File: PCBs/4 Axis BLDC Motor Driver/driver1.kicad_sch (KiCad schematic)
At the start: 13 parts, among them Q1 NMOS, Q2 NMOS, Q3 NMOS, Q4 NMOS, Q5 NMOS, Q6 NMOS, U2 DRV8301DCAR

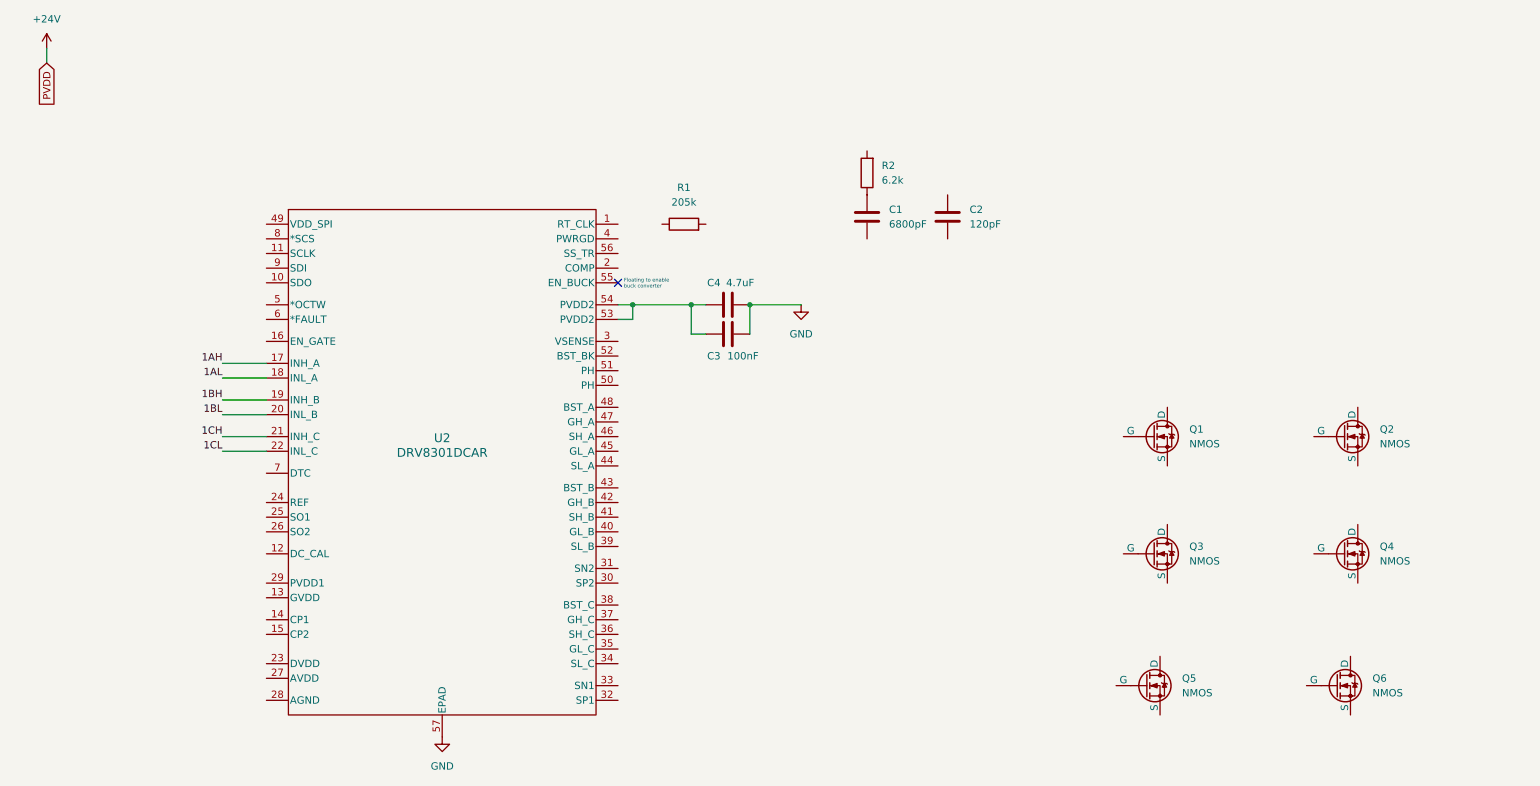
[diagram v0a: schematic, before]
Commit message: Add AMS1117 LDO to give 3.3V power to MCU
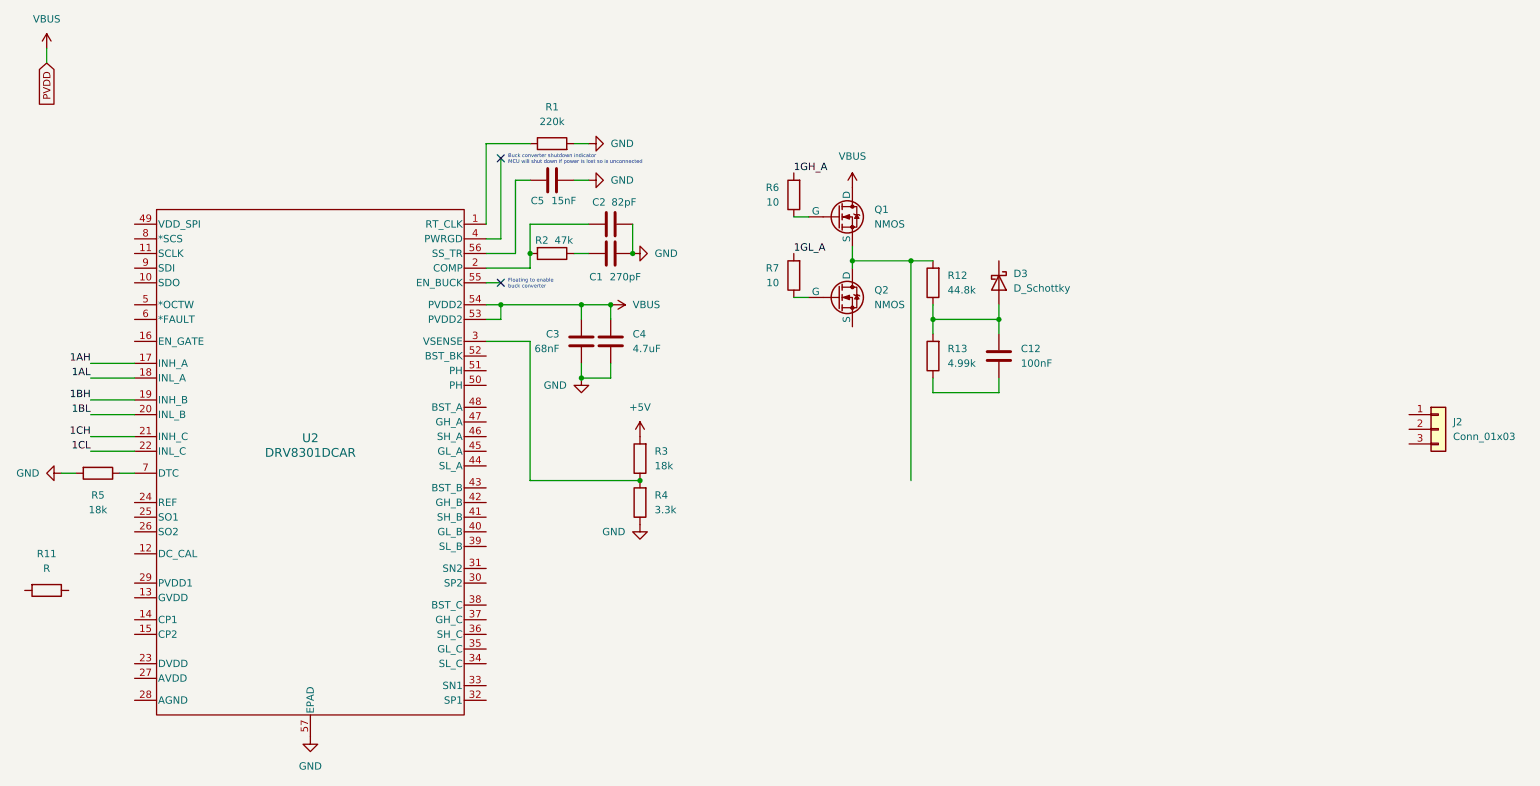
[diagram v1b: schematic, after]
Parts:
- removed Q3, Q4, Q5, Q6: NMOS, symbol Simulation_SPICE:NMOS
- added C12: 100nF, symbol Device:C
- added C5: 15nF, symbol Device:C
- added D3: D_Schottky, symbol Device:D_Schottky
- added J2: Conn_01x03, symbol Connector_Generic:Conn_01x03
- added R11: R, symbol Device:R
- added R12: 44.8k, symbol Device:R
- added R13: 4.99k, symbol Device:R
- added R3, R5: 18k, symbol Device:R
- added R4: 3.3k, symbol Device:R
- added R6, R7: 10, symbol Device:R
- C1: value 6800pF -> 270pF
- C2: value 120pF -> 82pF
- C3: value 100nF -> 68nF
- R1: value 205k -> 220k
- R2: value 6.2k -> 47k
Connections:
- net GND: now also C1.2, C2.2, C3.1, R1.2, C5.2, R4.1, R5.2; no longer C3.2
- net VBUS: now reaches C4.1, U2.53 (PVDD2), U2.54 (PVDD2)
- net VBUS: now also C3.2, Q1.1 (D); no longer C3.1
- net at Q2.1 (D): now also Q1.3 (S), R12.2
- net at Q2.2 (G): now also R7.1
- net at C2.1: now also R2.2, U2.2 (COMP)
- net at U2.1 (RT_CLK): now also R1.1
- net at U2.3 (VSENSE): now also R3.1, R4.2
- net at U2.56 (SS_TR): now also C5.1
- net at U2.7 (DTC): now also R5.1
- net at Q1.2 (G): now also R6.1
- new net: C12.1, D3.2 (A), R12.1, R13.2
- new net: C12.2, R13.1
- new net +5V: R3.2
- new net 1GH_A: R6.2
- new net 1GL_A: R7.2
- no-connect marks 1 -> 2
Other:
- note added: "Buck converter shutdown indicator MCU will shut down if power is lost so is unconnected"
- moved on the sheet: C1, C2, C3, C4, R1, U2
